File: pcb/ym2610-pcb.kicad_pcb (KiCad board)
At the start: 4 copper layers, 100.9 x 77.5 mm, 140 parts, among them J1 MIDI_IN, J2 LINE_OUT, J3 HEADPHONES, J4 SPDIF_COAX, J5 UART, SW1 BTN_A, SW2 BTN_B, SW3 CRESET, U1 YM2610, U10 TSV914IPT, U11 TSV914IPT, U12 AD8532, U13 74LVC2G08, U14 74AHCT595, U15 74AHCT595, U16 SPDIF_OPTICAL, U17 74HCT573, U18 TLP2361, U19 74HCT153, U2 YM3016, U20 74HCT153, U21 74LVC257, U3 74LVC1G34, U4 74LVC244, U5 74LV1T34, U6 74HCT573, U7 74HCT573, U8 74HCT153, U9 74HCT153

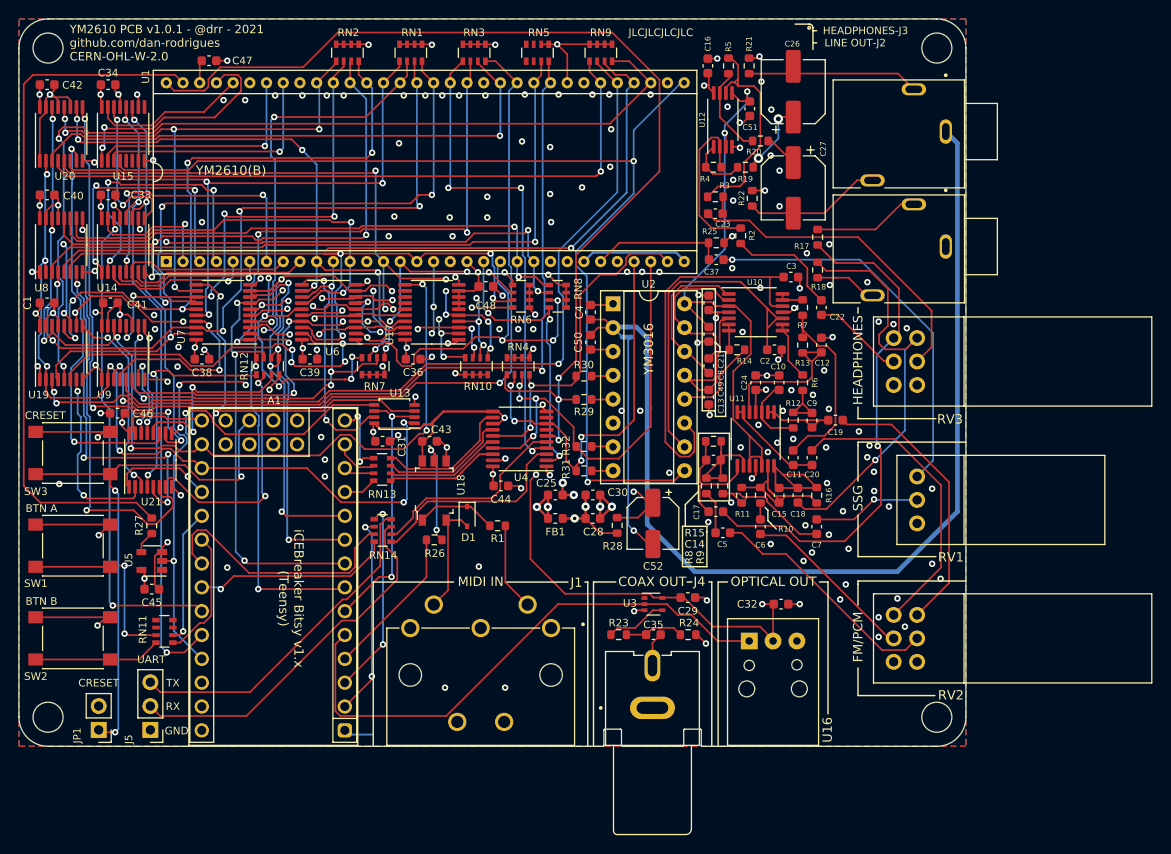
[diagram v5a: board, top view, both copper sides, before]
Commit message: pcb: v1.1.0
* Layout cleanup and removal of now-redundant parts
* Fixed lots of plane breakage near center of board
* Added 47pF caps to RMPX/PMPX
* Updated .pcf with reassigned pins
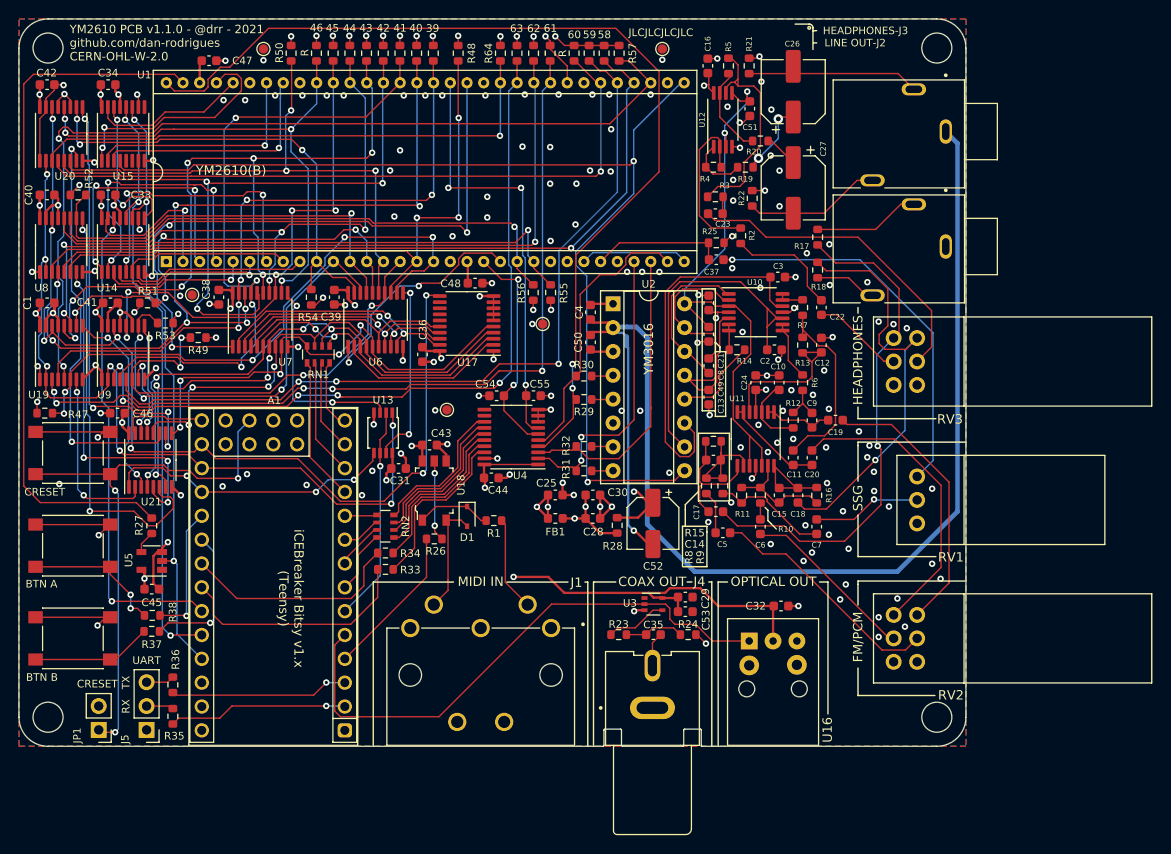
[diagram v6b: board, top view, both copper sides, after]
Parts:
- removed RN10, RN3, RN4, RN5, RN6, RN7, RN8, RN9: 100k, Resistor_SMD:R_Array_Convex_4x0603
- removed RN11, RN12, RN14: 100R, Resistor_SMD:R_Array_Convex_4x0603
- removed the RN2 at (52.5, 49.9)
- added C53: 10uF, Capacitor_SMD:C_0603_1608Metric, F.Cu at (88.5, 109.4)
- added C54: 47pF, Capacitor_SMD:C_0603_1608Metric, F.Cu at (68.4, 86.4)
- added C55: 47pF, Capacitor_SMD:C_0603_1608Metric, F.Cu at (72.3, 86.4)
- added R33: 100R, Resistor_SMD:R_0603_1608Metric, F.Cu at (56.5, 104.9)
- added R34: 100R, Resistor_SMD:R_0603_1608Metric, F.Cu at (56.5, 103.2)
- added R35: 100R, Resistor_SMD:R_0603_1608Metric, F.Cu at (33.9, 120.5)
- added R36: 100R, Resistor_SMD:R_0603_1608Metric, F.Cu at (33.9, 117.2)
- added R37: 100R, Resistor_SMD:R_0603_1608Metric, F.Cu at (31.6, 111.5)
- added R38: 100R, Resistor_SMD:R_0603_1608Metric, F.Cu at (31.7, 109.8)
- added R39: 100k, Resistor_SMD:R_0603_1608Metric, F.Cu at (61.6, 49.9)
- added R40: 100k, Resistor_SMD:R_0603_1608Metric, F.Cu at (59.9, 49.9)
- added R41: 100k, Resistor_SMD:R_0603_1608Metric, F.Cu at (58.1, 49.9)
- added R42: 100k, Resistor_SMD:R_0603_1608Metric, F.Cu at (56.3, 49.9)
- added R43: 100k, Resistor_SMD:R_0603_1608Metric, F.Cu at (54.5, 49.9)
- added R44: 100k, Resistor_SMD:R_0603_1608Metric, F.Cu at (52.8, 49.9)
- added R45: 100k, Resistor_SMD:R_0603_1608Metric, F.Cu at (51.0, 49.9)
- added R46: 100k, Resistor_SMD:R_0603_1608Metric, F.Cu at (49.2, 49.9)
- added R47: 100k, Resistor_SMD:R_0603_1608Metric, F.Cu at (20.2, 88.2)
- added R48: 100k, Resistor_SMD:R_0603_1608Metric, F.Cu at (64.3, 49.9)
- added R49: 100k, Resistor_SMD:R_0603_1608Metric, F.Cu at (36.6, 80.2)
- added R50: 100k, Resistor_SMD:R_0603_1608Metric, F.Cu at (46.5, 49.9)
- added R51: 100k, Resistor_SMD:R_0603_1608Metric, F.Cu at (31.2, 76.5)
- added R52: 100k, Resistor_SMD:R_0603_1608Metric, F.Cu at (23.8, 65.0)
- added R53: 100k, Resistor_SMD:R_0603_1608Metric, F.Cu at (33.1, 78.7)
- added R54: 100k, Resistor_SMD:R_0603_1608Metric, F.Cu at (48.6, 75.9)
- added R55: 100k, Resistor_SMD:R_0603_1608Metric, F.Cu at (74.2, 75.4)
- added R56: 100k, Resistor_SMD:R_0603_1608Metric, F.Cu at (72.3, 75.4)
- added R57: 100k, Resistor_SMD:R_0603_1608Metric, F.Cu at (81.5, 49.9)
- added R58: 100k, Resistor_SMD:R_0603_1608Metric, F.Cu at (79.8, 49.9)
- added R59: 100k, Resistor_SMD:R_0603_1608Metric, F.Cu at (78.2, 49.9)
- added R60: 100k, Resistor_SMD:R_0603_1608Metric, F.Cu at (76.7, 49.9)
- added R61: 100k, Resistor_SMD:R_0603_1608Metric, F.Cu at (74.1, 49.9)
- added R62: 100k, Resistor_SMD:R_0603_1608Metric, F.Cu at (72.3, 49.9)
- added R63: 100k, Resistor_SMD:R_0603_1608Metric, F.Cu at (70.6, 49.9)
- added R64: 100k, Resistor_SMD:R_0603_1608Metric, F.Cu at (68.8, 49.9)
- added TP1: TestPoint, TestPoint:TestPoint_Pad_D1.0mm, F.Cu at (43.5, 49.5)
- added TP2: TestPoint, TestPoint:TestPoint_Pad_D1.0mm, F.Cu at (86.0, 49.5)
- added TP3: TestPoint, TestPoint:TestPoint_Pad_D1.0mm, F.Cu at (73.3, 78.8)
- added TP4: TestPoint, TestPoint:TestPoint_Pad_D1.0mm, F.Cu at (36.0, 75.7)
- added TP5: TestPoint, TestPoint:TestPoint_Pad_D1.0mm, F.Cu at (63.1, 87.9)
- RN1: value 100k -> 100R
- U4: value 74LVC244 -> 74LVCH245
- moved RN1 33.6 mm to (49.4, 82.0), turned to 90 degrees
- moved C39 7.09 mm to (51.1, 75.9), turned to 90 degrees
- moved C38 6.84 mm to (38.8, 75.9), turned to 90 degrees
- moved RN2 6.06 mm to (56.5, 100.3)
- moved U6 5.06 mm to (55.5, 78.3), turned to 90 degrees
- moved U7 4.03 mm to (43.2, 78.3), turned to 90 degrees
- moved U17 3.89 mm to (65.2, 78.7)
- moved C31 3.36 mm to (58.0, 94.2)
- moved U13 2.33 mm to (56.3, 90.3), turned to 270 degrees
- moved C3 1.40 mm to (98.3, 73.8)
- moved C44 1.33 mm to (67.8, 95.2)
- moved C48 1.20 mm to (66.1, 74.4)
- moved C36 1.12 mm to (60.5, 82.0), turned to 270 degrees
- moved U4 0.91 mm to (70.0, 90.8)
- moved R1 0.68 mm to (68.1, 99.7)
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- renumbered RN13 to RN2
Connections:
- A1 pad 10: /YM_IO_3 -> /PMPX_3V3
- A1 pad 11: /RMPX_3V3 -> Net-(A1-Pad11)
- A1 pad 12: /PMPX_3V3 -> Net-(A1-Pad12)
- A1 pad 13: /DAC_CLK_3V3 -> Net-(A1-Pad13)
- A1 pad 14: /DAC_SH1_3V3 -> Net-(A1-Pad14)
- A1 pad 21: /DAC_SO_3V3 -> /DAC_SH2_3V3
- A1 pad 22: /DAC_SH2_3V3 -> /DAC_SH1_3V3
- A1 pad 7: /YM_IO_0 -> /DAC_CLK_3V3
- A1 pad 8: /YM_IO_1 -> /DAC_SO_3V3
- A1 pad 9: /YM_IO_2 -> /RMPX_3V3
- J5 pad 2: /UART_RX_HEADER -> Net-(J5-Pad2)
- J5 pad 3: /UART_TX_HEADER -> Net-(J5-Pad3)
- RN1 pad 1: +5V -> Net-(A1-Pad11)
- RN1 pad 2: +5V -> Net-(A1-Pad12)
- RN1 pad 3: +5V -> Net-(A1-Pad13)
- RN1 pad 4: +5V -> Net-(A1-Pad14)
- RN1 pad 5: /PAD3 -> /YM_IO_0
- RN1 pad 6: /PAD2 -> /YM_IO_1
- RN1 pad 7: /PAD1 -> /YM_IO_2
- RN1 pad 8: /PAD0 -> /YM_IO_3
- RN2 pad 1: Net-(RN13-Pad1) -> Net-(RN2-Pad1)
- RN2 pad 2: Net-(RN13-Pad2) -> Net-(RN2-Pad2)
- RN2 pad 4: Net-(RN13-Pad4) -> Net-(RN2-Pad4)
- RN2 pad 5: /DAC_SH1_3V3 -> /PMPX_3V3
- RN2 pad 6: /DAC_CLK_3V3 -> /RMPX_3V3
- RN2 pad 7: /PMPX_3V3 -> /DAC_SO_3V3
- RN2 pad 8: /RMPX_3V3 -> /DAC_CLK_3V3
- U17 pad 6: +5V -> GND
- U17 pad 7: +5V -> GND
- U17 pad 8: +5V -> GND
- U17 pad 9: +5V -> GND
- U21 pad 12: Net-(RN12-Pad3) -> /YM_IO_2
- U21 pad 4: Net-(RN12-Pad1) -> /YM_IO_0
- U21 pad 7: Net-(RN12-Pad2) -> /YM_IO_1
- U21 pad 9: Net-(RN12-Pad4) -> /YM_IO_3
- U4 pad 1: GND -> +3V3
- U4 pad 11: +3V3 -> Net-(U4-Pad11)
- U4 pad 12: Net-(RN13-Pad4) -> Net-(U4-Pad12)
- U4 pad 13: +3V3 -> Net-(RN2-Pad4)
- U4 pad 15: /DAC_SO -> Net-(RN2-Pad2)
- U4 pad 16: Net-(RN13-Pad2) -> Net-(RN2-Pad1)
- U4 pad 17: /DAC_SH2 -> Net-(R34-Pad2)
- U4 pad 18: Net-(RN13-Pad1) -> Net-(R33-Pad2)
- U4 pad 2: /RMPX -> /DAC_SH1
- U4 pad 3: Net-(RN14-Pad1) -> /DAC_SH2
- U4 pad 4: /PMPX -> /DAC_CLK
- U4 pad 5: Net-(RN14-Pad2) -> /DAC_SO
- U4 pad 6: /DAC_CLK -> /RMPX
- U4 pad 7: Net-(U4-Pad7) -> /PMPX
- U4 pad 8: /DAC_SH1 -> GND
- U4 pad 9: Net-(U4-Pad9) -> GND
- U6 pad 12: /RAD7 -> /RAD0
- U6 pad 13: /RAD6 -> /RAD1
- U6 pad 14: /RAD5 -> /RAD2
- U6 pad 15: /RAD4 -> /RAD3
- U6 pad 16: /RAD3 -> /RAD4
- U6 pad 17: /RAD2 -> /RAD5
- U6 pad 18: /RAD1 -> /RAD6
- U6 pad 19: /RAD0 -> /RAD7
- U6 pad 2: Net-(U17-Pad19) -> /YM_IO_0
- U6 pad 3: Net-(U17-Pad18) -> /YM_IO_1
- U6 pad 4: Net-(U17-Pad17) -> /YM_IO_2
- U6 pad 5: Net-(U17-Pad16) -> /YM_IO_3
- U6 pad 6: /YM_IO_0 -> Net-(U17-Pad16)
- U6 pad 7: /YM_IO_1 -> Net-(U17-Pad17)
- U6 pad 8: /YM_IO_2 -> Net-(U17-Pad18)
- U6 pad 9: /YM_IO_3 -> Net-(U17-Pad19)
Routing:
- net /UART_RX_HEADER: track 39.3 -> 0.00 mm
- net /UART_TX_HEADER: track 36.3 -> 0.00 mm
- net Net-(RN12-Pad2): track 26.2 -> 0.00 mm, vias 2 -> 0
- net Net-(RN12-Pad1): track 24.0 -> 0.00 mm, vias 2 -> 0
- net /DAC_SO_3V3: track 28.4 -> 5.17 mm
- net Net-(RN14-Pad1): track 22.7 -> 0.00 mm
- net Net-(RN14-Pad2): track 22.2 -> 0.00 mm
- net Net-(RN12-Pad3): track 20.1 -> 0.00 mm, vias 2 -> 0
- net Net-(R33-Pad2): track 0.00 -> 18.5 mm
- net /YM_IO_2: track 70.6 -> 52.4 mm, vias 8 -> 4
- net Net-(RN12-Pad4): track 17.9 -> 0.00 mm, vias 4 -> 0
- net /YM_IO_3: track 69.0 -> 51.4 mm, vias 8 -> 5
- net /DAC_SH1_3V3: track 8.10 -> 25.6 mm, vias 2 -> 0
- net Net-(R34-Pad2): track 0.00 -> 17.3 mm
- net /YM_IO_1: track 77.9 -> 60.7 mm, vias 9 -> 6
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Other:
- net class Default: trace_width 0.185 -> 0.15
- rule trace_min: 0.185 -> 0.15
- board text added: "R"
- board text added: "YM2610 PCB v1.1.0 - @drr - 2021 github.com/dan-rodrigues CERN-OHL-W-2.0"
- board text removed: "GND"
- board text removed: "YM2610 PCB v1.0.1 - @drr - 2021 github.com/dan-rodrigues CERN-OHL-W-2.0"
